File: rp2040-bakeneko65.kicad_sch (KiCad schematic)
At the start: 7 parts, among them SW1 SW_Push, U1 W25Q128JVS, U3 RP2040

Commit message: Add crystal
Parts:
- added C2, C3: 22pF, symbol Device:C_Small
- added R8: 1k, symbol Device:R_Small
- added Y1: 12MHz, symbol Device:Crystal_GND24_Small
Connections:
- net GND: now also C2.1, C3.1, Y1.2, Y1.4
- net XTAL_IN: now also C2.2, Y1.3
- net XTAL_OUT: now also R8.2
- new net: C3.2, R8.1, Y1.1
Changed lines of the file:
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@@
   (junction (at 46.99 36.83) (diameter 0) (color 0 0 0 0)
   )
+  (junction (at 121.285 69.215) (diameter 0) (color 0 0 0 0)
+  )
   (junction (at 68.58 29.21) (diameter 0) (color 0 0 0 0)
   )
+  (junction (at 137.16 69.215) (diameter 0) (color 0 0 0 0)
+  )
+  (junction (at 137.16 71.755) (diameter 0) (color 0 0 0 0)
+  )
+  (junction (at 137.16 64.135) (diameter 0) (color 0 0 0 0)
+  )
   (junction (at 138.43 22.86) (diameter 0) (color 0 0 0 0)
   )
@@
     (stroke (width 0) (type default) (color 0 0 0 0))
   )
+  (wire (pts (xy 134.62 71.755) (xy 137.16 71.755))
+    (stroke (width 0) (type default) (color 0 0 0 0))
+  )
+  (wire (pts (xy 134.62 66.675) (xy 134.62 71.755))
+    (stroke (width 0) (type default) (color 0 0 0 0))
+  )
   (wire (pts (xy 76.2 26.67) (xy 76.2 29.21))
     (stroke (width 0) (type default) (color 0 0 0 0))
   )
   (wire (pts (xy 45.72 82.55) (xy 48.26 82.55))
+    (stroke (width 0) (type default) (color 0 0 0 0))
+  )
+  (wire (pts (xy 128.905 69.215) (xy 137.16 69.215))
     (stroke (width 0) (type default) (color 0 0 0 0))
   )
@@
     (stroke (width 0) (type solid) (color 0 0 0 0))
   )
+  (wire (pts (xy 139.7 71.755) (xy 137.16 71.755))
+    (stroke (width 0) (type default) (color 0 0 0 0))
+  )
   (wire (pts (xy 69.85 120.65) (xy 73.66 120.65))
     (stroke (width 0) (type default) (color 0 0 0 0))
@@
     (stroke (width 0) (type solid) (color 0 0 0 0))
   )
+  (wire (pts (xy 123.825 69.215) (xy 121.285 69.215))
+    (stroke (width 0) (type default) (color 0 0 0 0))
+  )
   (wire (pts (xy 34.29 35.56) (xy 30.48 35.56))
     (stroke (width 0) (type default) (color 0 0 0 0))
@@
     (stroke (width 0) (type default) (color 0 0 0 0))
   )
+  (wire (pts (xy 121.285 69.215) (xy 121.285 71.755))
+    (stroke (width 0) (type default) (color 0 0 0 0))
+  )
+  (wire (pts (xy 121.285 69.215) (xy 121.285 64.135))
+    (stroke (width 0) (type default) (color 0 0 0 0))
+  )
   (wire (pts (xy 45.72 92.71) (xy 48.26 92.71))
     (stroke (width 0) (type default) (color 0 0 0 0))
@@
     (stroke (width 0) (type default) (color 0 0 0 0))
   )
+  (wire (pts (xy 128.905 64.135) (xy 137.16 64.135))
+    (stroke (width 0) (type default) (color 0 0 0 0))
+  )
   (wire (pts (xy 138.43 43.18) (xy 138.43 45.72))
     (stroke (width 0) (type default) (color 0 0 0 0))
   )
   (wire (pts (xy 34.29 46.99) (xy 38.1 46.99))
+    (stroke (width 0) (type default) (color 0 0 0 0))
+  )
+  (wire (pts (xy 149.225 69.215) (xy 153.035 69.215))
     (stroke (width 0) (type default) (color 0 0 0 0))
   )
@@
     (stroke (width 0) (type solid) (color 0 0 0 0))
   )
+  (wire (pts (xy 121.285 64.135) (xy 123.825 64.135))
+    (stroke (width 0) (type default) (color 0 0 0 0))
+  )
   (wire (pts (xy 46.99 24.13) (xy 46.99 26.67))
     (stroke (width 0) (type default) (color 0 0 0 0))
   )
   (wire (pts (xy 46.99 36.83) (xy 48.26 36.83))
+    (stroke (width 0) (type default) (color 0 0 0 0))
+  )
+  (wire (pts (xy 137.16 64.135) (xy 153.035 64.135))
+    (stroke (width 0) (type default) (color 0 0 0 0))
+  )
+  (wire (pts (xy 139.7 66.675) (xy 139.7 71.755))
     (stroke (width 0) (type default) (color 0 0 0 0))
   )
@@
   )
   (polyline (pts (xy 107.95 53.975) (xy 107.95 50.8))
-    (stroke (width 0) (type default) (color 0 0 0 0))
+    (stroke (width 0) (type solid) (color 0 0 0 0))
   )
   (wire (pts (xy 68.58 26.67) (xy 68.58 29.21))
@@
   )
   (wire (pts (xy 44.45 36.83) (xy 46.99 36.83))
+    (stroke (width 0) (type default) (color 0 0 0 0))
+  )
+  (wire (pts (xy 137.16 69.215) (xy 144.145 69.215))
     (stroke (width 0) (type default) (color 0 0 0 0))
   )
@@
     )
   )
+  (global_label "XTAL_IN" (shape input) (at 153.035 64.135 0) (fields_autoplaced)
+    (effects (font (size 1.27 1.27)) (justify left))
+    (property "Intersheet References" "${INTERSHEET_REFS}" (id 0) (at 162.6448 64.0556 0)
+      (effects (font (size 1.27 1.27)) (justify left) hide)
+    )
+  )
   (global_label "SD0" (shape input) (at 48.26 59.69 180) (fields_autoplaced)
     (effects (font (size 1.27 1.27)) (justify right))
@@
     (property "Intersheet References" "${INTERSHEET_REFS}" (id 0) (at 114.3664 35.4806 0)
       (effects (font (size 1.27 1.27)) (justify right) hide)
+    )
+  )
+  (global_label "XTAL_OUT" (shape input) (at 153.035 69.215 0) (fields_autoplaced)
+    (effects (font (size 1.27 1.27)) (justify left))
+    (property "Intersheet References" "${INTERSHEET_REFS}" (id 0) (at 164.3381 69.1356 0)
+      (effects (font (size 1.27 1.27)) (justify left) hide)
     )
   )
@@
     (pin "1")
   )
+  (symbol (lib_id "Device:Crystal_GND24_Small") (at 137.16 66.675 90) (unit 1)
+    (in_bom yes) (on_board yes)
+    (property "Reference" "Y1" (id 0) (at 141.605 71.12 90))
+    (property "Value" "12MHz" (id 1) (at 143.51 73.66 90))
+    (property "Footprint" "" (id 2) (at 137.16 66.675 0)
+      (effects (font (size 1.27 1.27)) hide)
+    )
+    (property "Datasheet" "~" (id 3) (at 137.16 66.675 0)
+      (effects (font (size 1.27 1.27)) hide)
+    )
+    (pin "1")
+    (pin "2")
+    (pin "3")
+    (pin "4")
+  )
   (symbol (lib_id "power:+3V3") (at 133.985 22.86 0) (unit 1)
     (in_bom yes) (on_board yes) (fields_autoplaced)
@@
     (pin "1")
   )
+  (symbol (lib_id "power:GND") (at 137.16 71.755 0) (unit 1)
+    (in_bom yes) (on_board yes) (fields_autoplaced)
+    (property "Reference" "#PWR?" (id 0) (at 137.16 78.105 0)
+      (effects (font (size 1.27 1.27)) hide)
+    )
+    (property "Value" "GND" (id 1) (at 137.16 76.2 0))
+    (property "Footprint" "" (id 2) (at 137.16 71.755 0)
+      (effects (font (size 1.27 1.27)) hide)
+    )
+    (property "Datasheet" "" (id 3) (at 137.16 71.755 0)
+      (effects (font (size 1.27 1.27)) hide)
+    )
+    (pin "1")
+  )
   (symbol (lib_id "power:GND") (at 138.43 45.72 0) (unit 1)
     (in_bom yes) (on_board yes) (fields_autoplaced)
@@
     )
     (pin "1")
+  )
+  (symbol (lib_id "Device:C_Small") (at 126.365 64.135 90) (unit 1)
+    (in_bom yes) (on_board yes)
+    (property "Reference" "C2" (id 0) (at 123.19 62.23 90))
+    (property "Value" "22pF" (id 1) (at 130.175 67.31 90))
+    (property "Footprint" "" (id 2) (at 126.365 64.135 0)
+      (effects (font (size 1.27 1.27)) hide)
+    )
+    (property "Datasheet" "~" (id 3) (at 126.365 64.135 0)
+      (effects (font (size 1.27 1.27)) hide)
+    )
+    (pin "1")
+    (pin "2")
   )
   (symbol (lib_id "MCU_RaspberryPi:RP2040") (at 73.66 74.93 0) (unit 1)
@@
     (pin "1")
   )
+  (symbol (lib_id "power:GND") (at 121.285 71.755 0) (unit 1)
+    (in_bom yes) (on_board yes) (fields_autoplaced)
+    (property "Reference" "#PWR?" (id 0) (at 121.285 78.105 0)
+      (effects (font (size 1.27 1.27)) hide)
+    )
+    (property "Value" "GND" (id 1) (at 121.285 76.2 0))
+    (property "Footprint" "" (id 2) (at 121.285 71.755 0)
+      (effects (font (size 1.27 1.27)) hide)
+    )
+    (property "Datasheet" "" (id 3) (at 121.285 71.755 0)
+      (effects (font (size 1.27 1.27)) hide)
+    )
+    (pin "1")
+  )
   (symbol (lib_id "Switch:SW_Push") (at 39.37 36.83 0) (unit 1)
     (in_bom yes) (on_board yes) (fields_autoplaced)
@@
     )
     (property "Datasheet" "~" (id 3) (at 39.37 31.75 0)
+      (effects (font (size 1.27 1.27)) hide)
+    )
+    (pin "1")
+    (pin "2")
+  )
+  (symbol (lib_id "Device:R_Small") (at 146.685 69.215 90) (unit 1)
+    (in_bom yes) (on_board yes)
+    (property "Reference" "R8" (id 0) (at 146.685 66.675 90))
+    (property "Value" "1k" (id 1) (at 146.685 71.755 90))
+    (property "Footprint" "" (id 2) (at 146.685 69.215 0)
+      (effects (font (size 1.27 1.27)) hide)
+    )
+    (property "Datasheet" "~" (id 3) (at 146.685 69.215 0)
       (effects (font (size 1.27 1.27)) hide)
     )
@@
     (pin "8")
   )
+  (symbol (lib_id "Device:C_Small") (at 126.365 69.215 90) (unit 1)
+    (in_bom yes) (on_board yes)
+    (property "Reference" "C3" (id 0) (at 123.19 67.31 90))
+    (property "Value" "22pF" (id 1) (at 130.175 62.23 90))
+    (property "Footprint" "" (id 2) (at 126.365 69.215 0)
+      (effects (font (size 1.27 1.27)) hide)
+    )
+    (property "Datasheet" "~" (id 3) (at 126.365 69.215 0)
+      (effects (font (size 1.27 1.27)) hide)
+    )
+    (pin "1")
+    (pin "2")
+  )
   (symbol (lib_id "Device:R_Small") (at 40.64 44.45 90) (unit 1)
     (in_bom yes) (on_board yes)
@@
       (reference "#PWR?") (unit 1) (value "GND") (footprint "")
     )
+    (path "/4d7af9ba-56f7-4f23-80f9-8059105eceaf"
+      (reference "#PWR?") (unit 1) (value "GND") (footprint "")
+    )
     (path "/6a98ce06-492e-4d48-aec8-372ade077156"
       (reference "#PWR?") (unit 1) (value "GND") (footprint "")
@@
       (reference "#PWR?") (unit 1) (value "+1V1") (footprint "")
     )
+    (path "/87f8dc13-16f4-4f84-9e25-bb68f2773d2a"
+      (reference "#PWR?") (unit 1) (value "GND") (footprint "")
+    )
     (path "/bd94dd6f-78e2-42d1-b9ab-bcf0e0b718a5"
       (reference "#PWR?") (unit 1) (value "GND") (footprint "")
@@
       (reference "C1") (unit 1) (value "100nF") (footprint "")
     )
+    (path "/6fb39cf3-b34f-48ed-8269-92a74e022ac6"
+      (reference "C2") (unit 1) (value "22pF") (footprint "")
+    )
+    (path "/d7f16c51-5ec8-43c4-8574-fdd730659a8f"
+      (reference "C3") (unit 1) (value "22pF") (footprint "")
+    )
     (path "/e82e7d2b-ad35-4be9-a59e-016eb5a2e0c6"
       (reference "R5") (unit 1) (value "27") (footprint "")
@@
       (reference "R7") (unit 1) (value "10k") (footprint "")
     )
+    (path "/9883a342-199d-4e3a-a95e-b26712831769"
+      (reference "R8") (unit 1) (value "1k") (footprint "")
+    )
     (path "/9769ce52-6e73-4db2-bb86-cd67bfc206bf"
       (reference "SW1") (unit 1) (value "SW_Push") (footprint "")
@@
       (reference "U3") (unit 1) (value "RP2040") (footprint "Package_DFN_QFN:QFN-56-1EP_7x7mm_P0.4mm_EP3.2x3.2mm")
     )
-  )
+    (path "/278eb6a6-e06a-45b7-ad35-f1eaa2ac3e09"
+      (reference "Y1") (unit 1) (value "12MHz") (footprint "")
+    )
+  )

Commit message: Some line stuff
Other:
- note added: "Crystal"
- note added: "Flash"
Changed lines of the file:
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@@
     (stroke (width 0) (type default) (color 0 0 0 0))
+  )
+  (polyline (pts (xy 165.1 53.34) (xy 107.95 53.34))
+    (stroke (width 0) (type solid) (color 0 0 0 0))
   )
   (wire (pts (xy 76.2 26.67) (xy 76.2 29.21))
@@
     (stroke (width 0) (type default) (color 0 0 0 0))
   )
-  (polyline (pts (xy 107.95 12.7) (xy 165.1 12.7))
-    (stroke (width 0) (type solid) (color 0 0 0 0))
-  )
-  (polyline (pts (xy 165.1 53.975) (xy 107.95 53.975))
-    (stroke (width 0) (type solid) (color 0 0 0 0))
-  )
   (wire (pts (xy 139.7 71.755) (xy 137.16 71.755))
     (stroke (width 0) (type default) (color 0 0 0 0))
@@
     (stroke (width 0) (type default) (color 0 0 0 0))
   )
+  (polyline (pts (xy 107.95 53.34) (xy 107.95 82.55))
+    (stroke (width 0) (type solid) (color 0 0 0 0))
+  )
   (wire (pts (xy 46.99 31.75) (xy 46.99 36.83))
     (stroke (width 0) (type default) (color 0 0 0 0))
-  )
-  (polyline (pts (xy 165.1 12.7) (xy 165.1 50.8))
-    (stroke (width 0) (type solid) (color 0 0 0 0))
   )
   (wire (pts (xy 123.825 69.215) (xy 121.285 69.215))
@@
     (stroke (width 0) (type default) (color 0 0 0 0))
   )
+  (polyline (pts (xy 165.1 53.34) (xy 165.1 82.55))
+    (stroke (width 0) (type solid) (color 0 0 0 0))
+  )
   (wire (pts (xy 138.43 22.86) (xy 140.97 22.86))
     (stroke (width 0) (type default) (color 0 0 0 0))
@@
   (wire (pts (xy 128.905 64.135) (xy 137.16 64.135))
     (stroke (width 0) (type default) (color 0 0 0 0))
+  )
+  (polyline (pts (xy 107.95 12.7) (xy 165.1 12.7))
+    (stroke (width 0) (type solid) (color 0 0 0 0))
   )
   (wire (pts (xy 138.43 43.18) (xy 138.43 45.72))
@@
     (stroke (width 0) (type default) (color 0 0 0 0))
   )
-  (polyline (pts (xy 165.1 50.165) (xy 165.1 53.975))
-    (stroke (width 0) (type solid) (color 0 0 0 0))
-  )
   (wire (pts (xy 121.285 64.135) (xy 123.825 64.135))
     (stroke (width 0) (type default) (color 0 0 0 0))
@@
     (stroke (width 0) (type default) (color 0 0 0 0))
   )
+  (polyline (pts (xy 107.95 53.34) (xy 107.95 12.7))
+    (stroke (width 0) (type solid) (color 0 0 0 0))
+  )
   (wire (pts (xy 43.18 113.03) (xy 48.26 113.03))
     (stroke (width 0) (type default) (color 0 0 0 0))
@@
   (wire (pts (xy 81.28 29.21) (xy 83.82 29.21))
     (stroke (width 0) (type default) (color 0 0 0 0))
-  )
-  (polyline (pts (xy 107.95 12.7) (xy 107.95 50.8))
-    (stroke (width 0) (type solid) (color 0 0 0 0))
   )
   (wire (pts (xy 43.18 46.99) (xy 48.26 46.99))
@@
     (stroke (width 0) (type default) (color 0 0 0 0))
   )
-  (polyline (pts (xy 107.95 53.975) (xy 107.95 50.8))
-    (stroke (width 0) (type solid) (color 0 0 0 0))
-  )
   (wire (pts (xy 68.58 26.67) (xy 68.58 29.21))
     (stroke (width 0) (type default) (color 0 0 0 0))
+  )
+  (polyline (pts (xy 165.1 12.7) (xy 165.1 53.34))
+    (stroke (width 0) (type solid) (color 0 0 0 0))
   )
   (wire (pts (xy 44.45 36.83) (xy 46.99 36.83))
@@
     (stroke (width 0) (type default) (color 0 0 0 0))
   )
+  (polyline (pts (xy 165.1 82.55) (xy 107.95 82.55))
+    (stroke (width 0) (type solid) (color 0 0 0 0))
+  )
+  (text "Flash\n" (at 154.305 51.435 0)
+    (effects (font (size 1.27 1.27)) (justify left bottom))
+  )
+  (text "Crystal" (at 154.305 81.28 0)
+    (effects (font (size 1.27 1.27)) (justify left bottom))
+  )
   (global_label "XTAL_OUT" (shape input) (at 45.72 92.71 180) (fields_autoplaced)

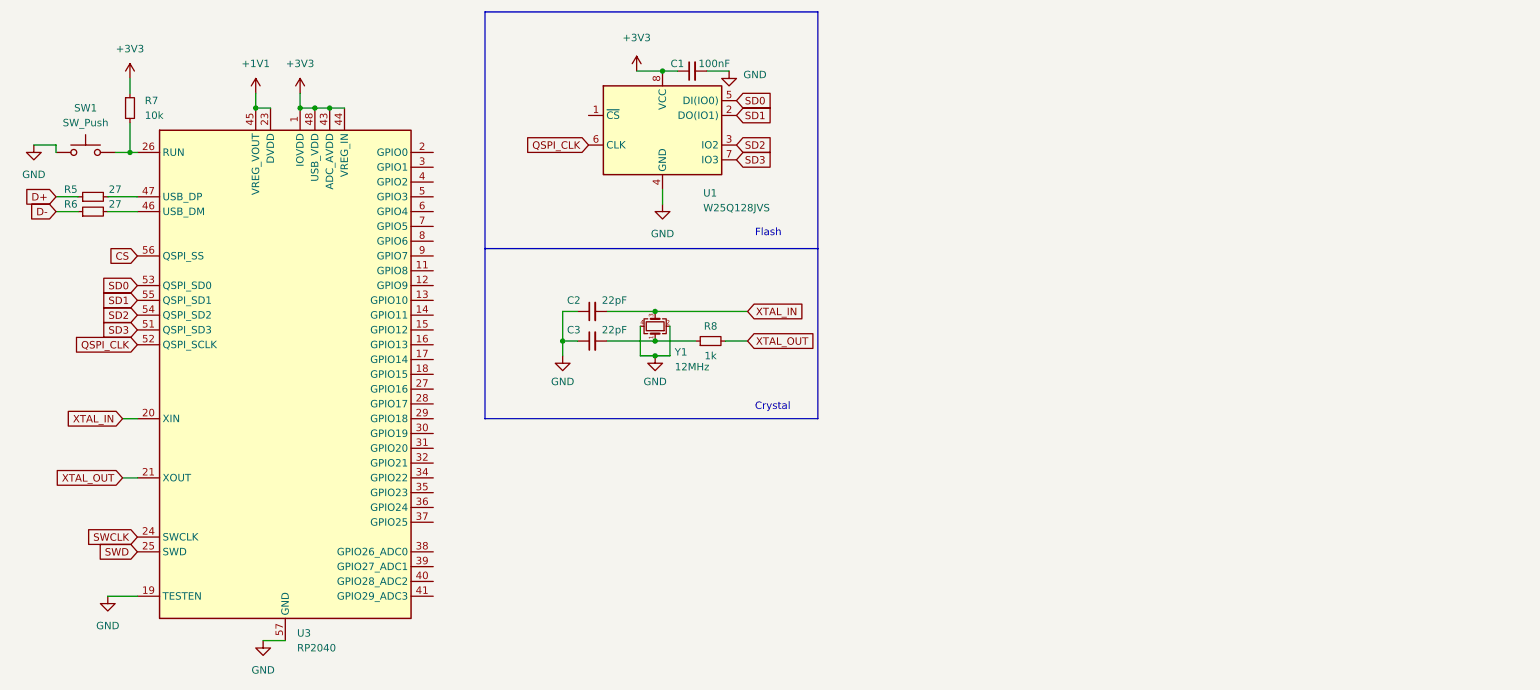
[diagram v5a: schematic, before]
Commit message: JST and voltage regulator
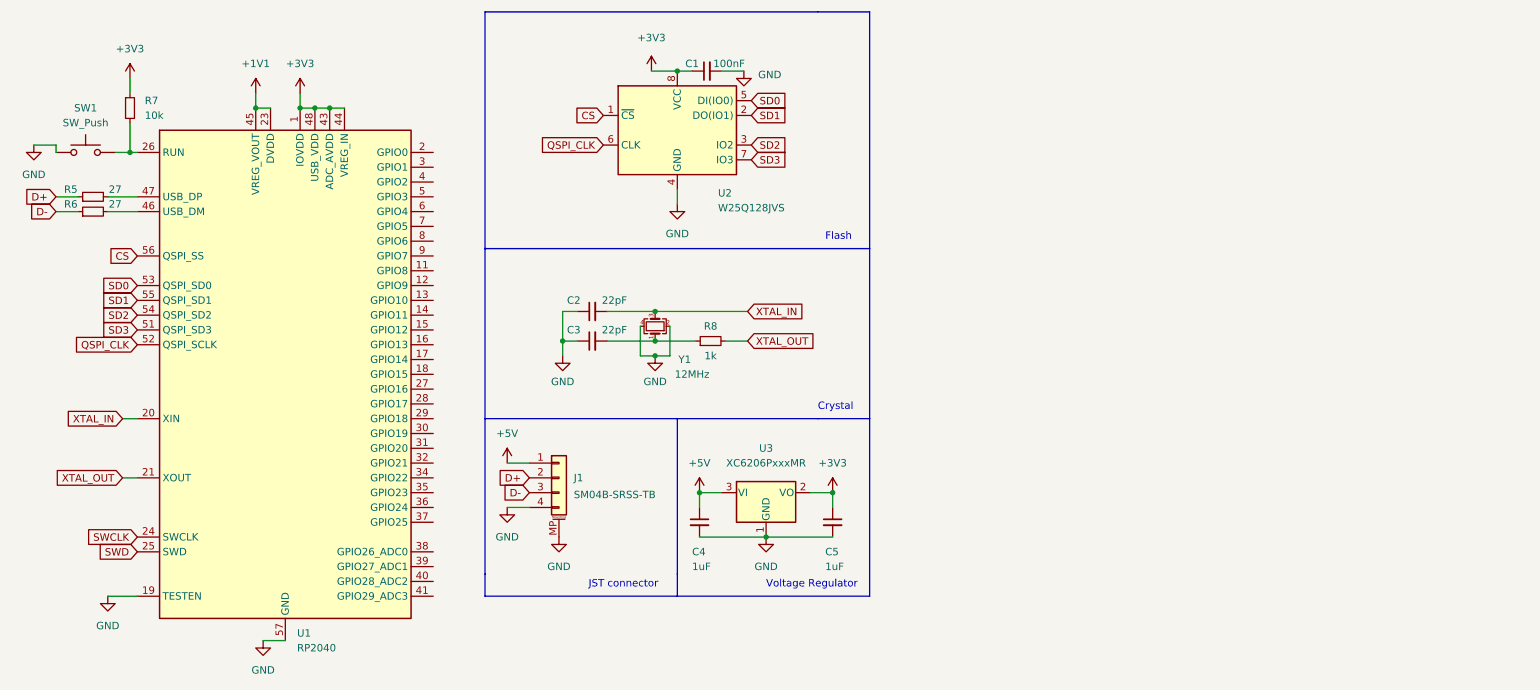
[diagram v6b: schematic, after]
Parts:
- added C4, C5: 1uF, symbol Device:C_Small
- added J1: SM04B-SRSS-TB, symbol Connector_Generic_MountingPin:Conn_01x04_MountingPin
- added U3: XC6206PxxxMR, Package_TO_SOT_SMD:SOT-23, symbol Regulator_Linear:XC6206PxxxMR
- renumbered U3 to U1, U1 to U2
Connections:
- net +3V3: now also C5.1, U3.2 (VO)
- net CS: now also U2.1 (~{CS})
- net D+: now also J1.2 (Pin_2)
- net D-: now also J1.3 (Pin_3)
- net GND: now also C4.2, C5.2, J1.4 (Pin_4), J1.MP (MountPin), U3.1 (GND)
- new net +5V: C4.1, J1.1 (Pin_1), U3.3 (VI)
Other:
- note added: "JST connector"
- note added: "Voltage Regulator"
- moved on the sheet: C1, U2

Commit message: Add decoupling capacitors
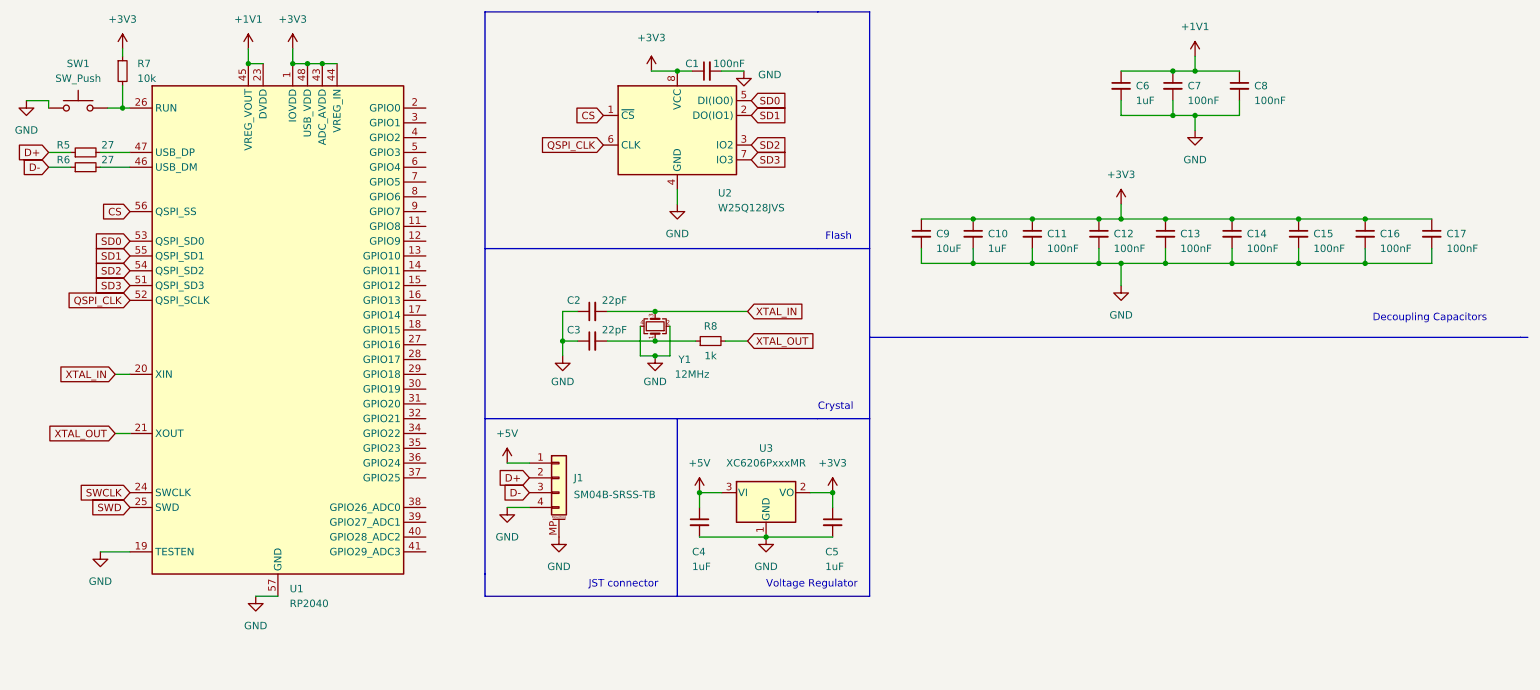
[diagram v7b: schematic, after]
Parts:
- added C10, C6: 1uF, symbol Device:C_Small
- added C11, C12, C13, C14, C15, C16, C17, C7, C8: 100nF, symbol Device:C_Small
- added C9: 10uF, symbol Device:C_Small
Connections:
- net +1V1: now also C6.1, C7.1, C8.1
- net +3V3: now also C10.1, C11.1, C12.1, C13.1, C14.1, C15.1, C16.1, C17.1, C9.1
- net GND: now also C10.2, C11.2, C12.2, C13.2, C14.2, C15.2, C16.2, C17.2, C6.2, C7.2, C8.2, C9.2
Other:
- note added: "Decoupling Capacitors"
- moved on the sheet: R5, R6, R7, SW1, U1
